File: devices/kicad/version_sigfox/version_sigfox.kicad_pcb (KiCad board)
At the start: 2 copper layers, 64.4 x 95.3 mm, 7 parts, among them U1 polulu, U2 esp32_NodeMCU-track_chip, U3 GPS_PA6H, U4 bmp180-track_chip, U7 charger_mr010

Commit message: fixing sigfox pcb
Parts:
- moved G*** 0.76 mm to (164.6, 127.3)
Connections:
- U2 pad 21: RX2 -> (no net)
- U2 pad 22: TX2 -> MCU_TX2
- U2 pad 27: (no net) -> GPS_TX0
- U2 pad 28: TX0 -> (no net)
- U3 pad 5: TX0 -> GPS_TX0
- wisol1 pad 1: TX2 -> (no net)
- wisol1 pad 2: RX2 -> MCU_TX2
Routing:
- net GPS_TX0: track 0.00 -> 26.3 mm
- net TX0: track 25.3 -> 0.00 mm
- net RX2: track 13.8 -> 0.00 mm
- net TX2: track 13.7 -> 0.00 mm
- net MCU_TX2: track 0.00 -> 12.7 mm

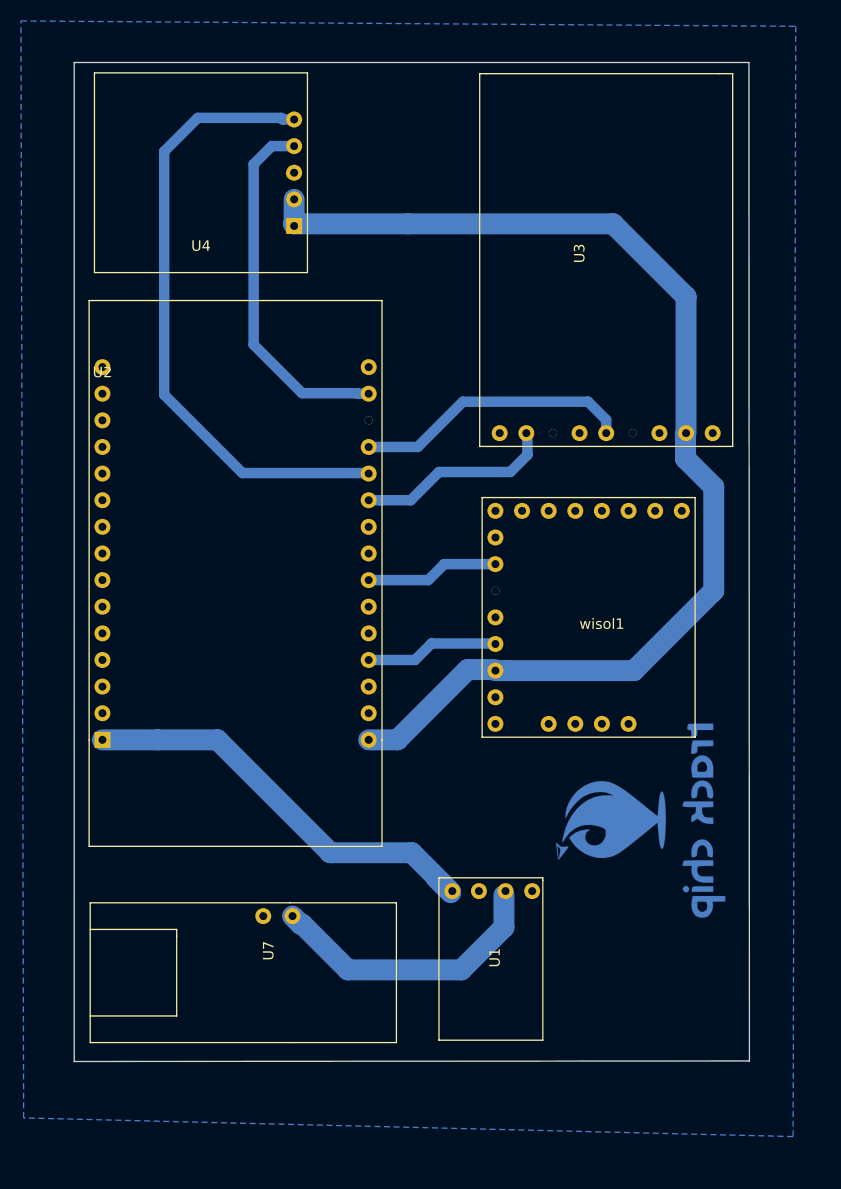
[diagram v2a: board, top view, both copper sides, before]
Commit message: correction symbole + empreinte sigfox
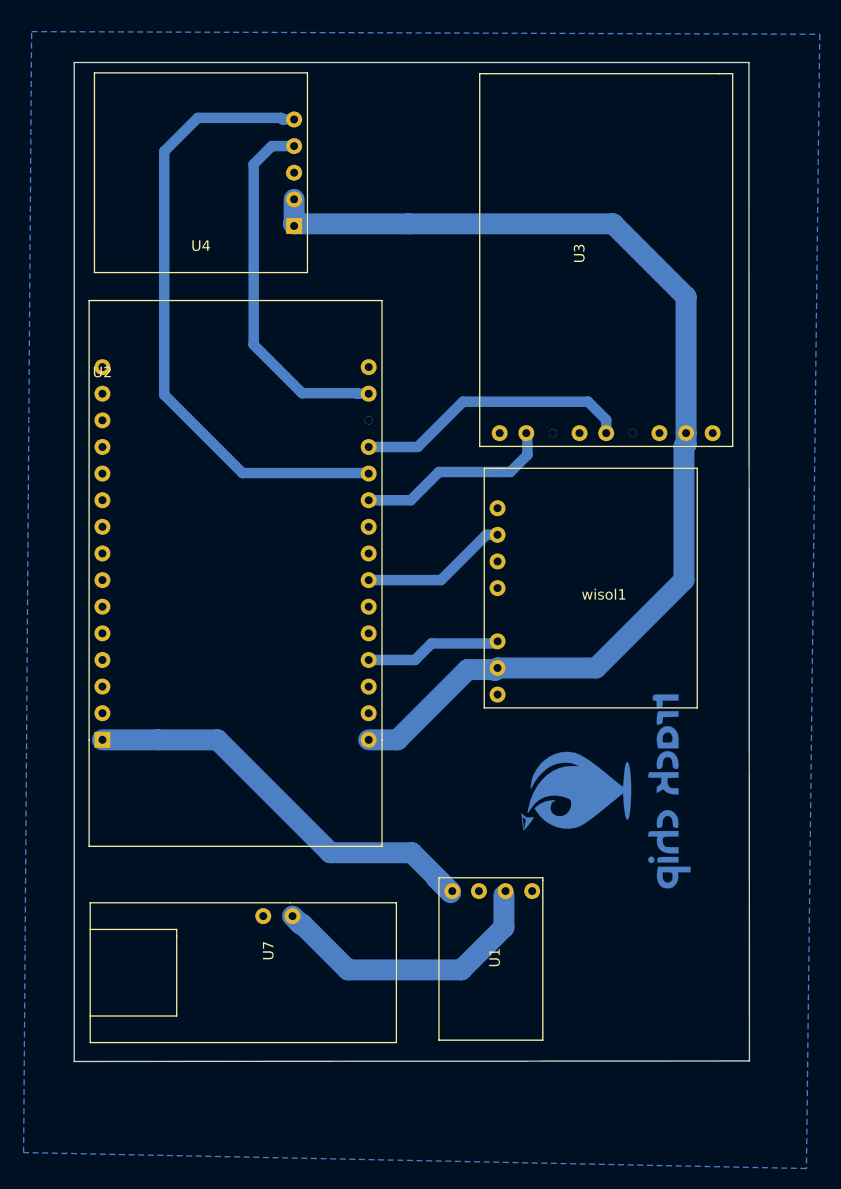
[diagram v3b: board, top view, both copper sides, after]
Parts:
- moved G*** 4.33 mm to (161.3, 124.5)
- moved wisol1 2.80 mm to (142.5, 91.7)
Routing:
- net 3V3: track 110.5 -> 106.1 mm
- net MCU_TX2: track 12.7 -> 14.2 mm
